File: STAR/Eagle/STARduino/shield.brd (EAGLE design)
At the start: 57.1 x 53.3 mm, 29 parts, among them U1 PCA9515A, U11 CC2, U12 SSCMNNN015PA2A3, U3 MAX31725MTA+, U5 DS3231MZ+, U7 BMX055, U8 ADXL375BCCZ

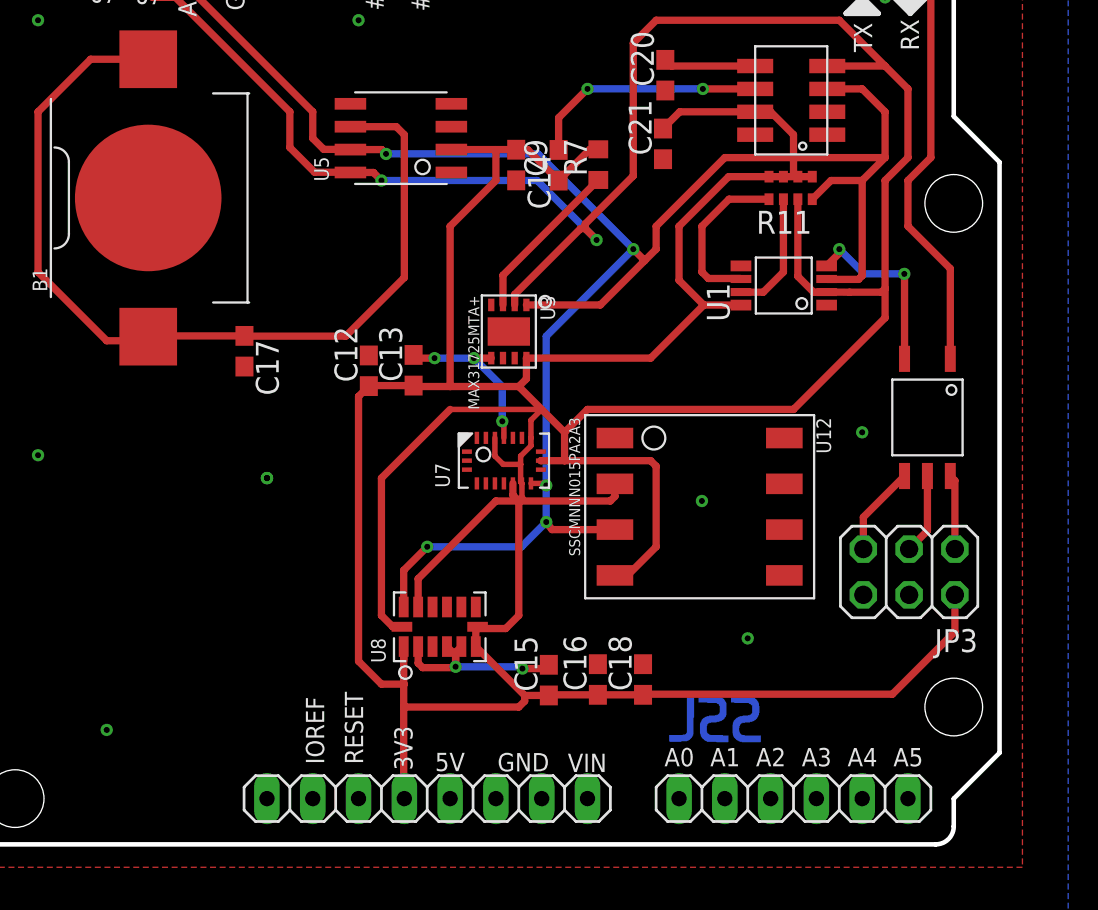
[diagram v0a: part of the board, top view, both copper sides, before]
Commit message: Fixed optoisolator circuit and added SPI header on top, but not yet the SPI head on the ICSP board. Fixed a lot of air wires
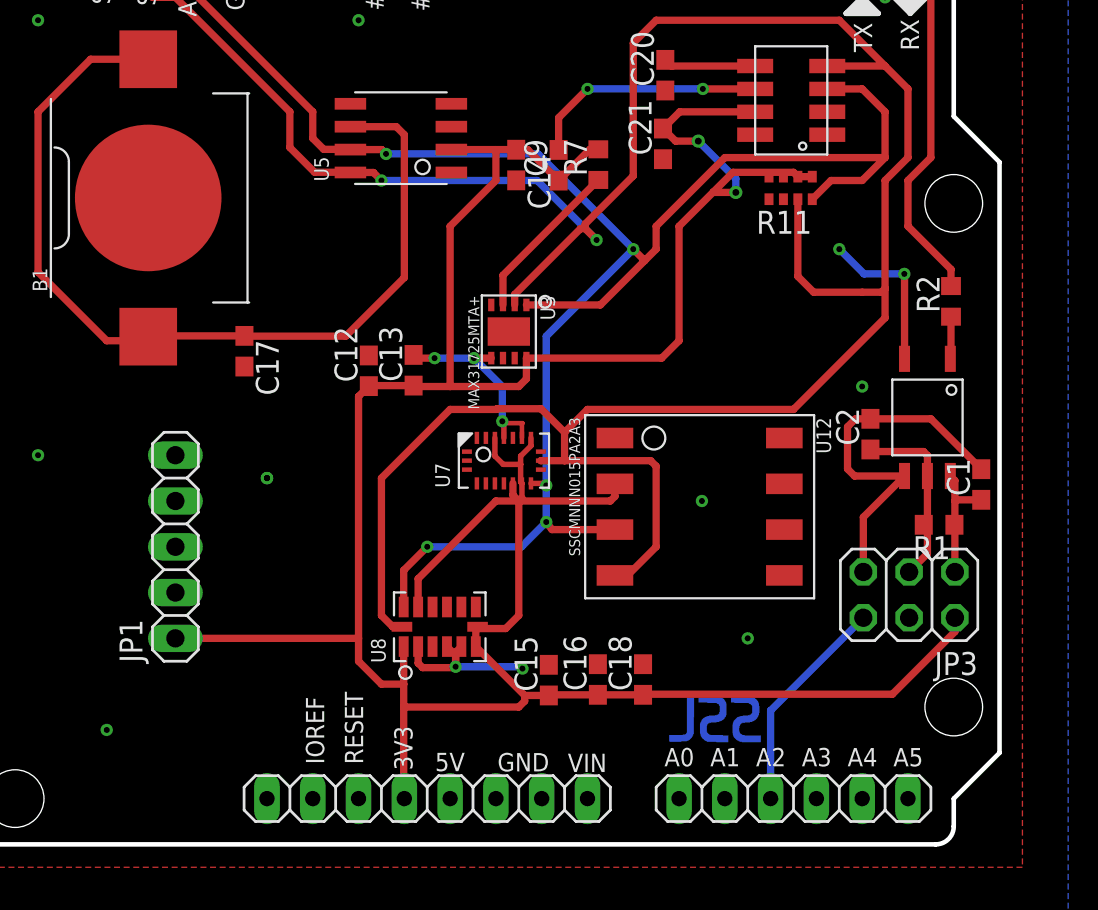
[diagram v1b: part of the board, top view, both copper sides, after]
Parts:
- removed U1: PCA9515A, CM_IC:TSSOP8
- added C1: 100nF, resistor:C0603
- added C2: 15pf, resistor:C0603
- added JP1: (no value), pinhead:1X05
- added R1, R2: 442, resistor:R0603
- moved JP3 1.27 mm to (63.6, 13.8)
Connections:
- removed net A2: AD.3
- removed net SCL_BUFF: R11.2, U1.P$7
- removed net SDA_BUFF: R11.1, U1.P$6
- new net MISO: JP1.3
- new net MOSI: JP1.4
- new net N$2: R2.1, U$3.P$1
- new net SCK: JP1.5
- net +3V3: now also JP1.1; no longer R11.7, R11.8, U1.P$8
- net BIAS_REF: now also AD.3
- net GND: now also JP1.2; no longer U1.P$4
- net MOTOR: now also R2.2; no longer U$3.P$1
- net MOTOR_GND: now also C1.2, C2.2
- net MOTOR_SIGNAL: now also C2.1, R1.2
- net MOTOR_VCC: now also C1.1, R1.1
- net SCL: no longer U1.P$2
- net SDA: no longer U1.P$3
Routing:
- net MOTOR_GND: track 5.00 -> 20.7 mm
- net BIAS_REF: track 0.00 -> 12.2 mm
- net SDA_BUFF: track 9.17 -> 0.00 mm
- net SDA: track 113.8 -> 105.0 mm
- net SCL_BUFF: track 6.86 -> 0.00 mm
- net MOTOR_SIGNAL: track 4.47 -> 10.4 mm
- net MOTOR: track 25.9 -> 21.9 mm
- net +3V3: track 173.7 -> 177.6 mm, vias 0 -> 2
- net MOTOR_VCC: track 4.16 -> 7.21 mm
- net N$2: track 0.00 -> 2.35 mm
- net GND: track 44.3 -> 43.0 mm

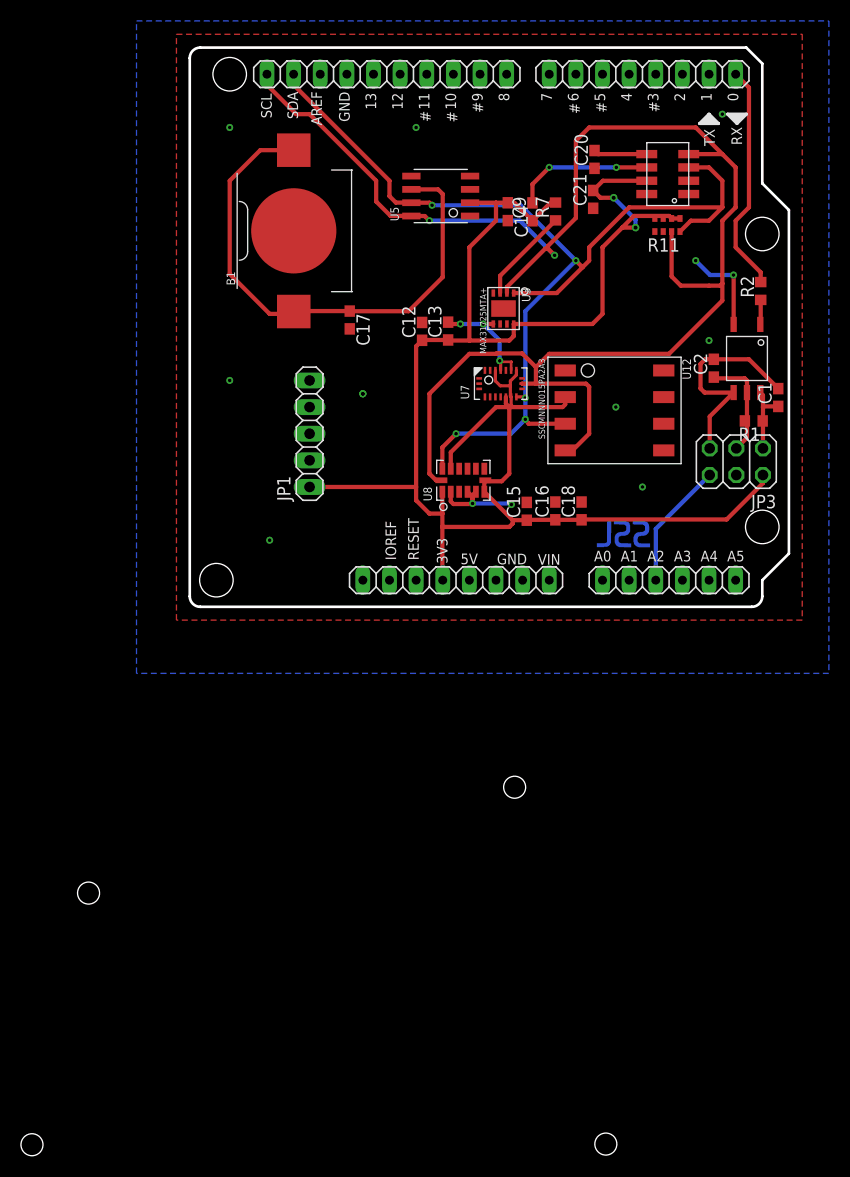
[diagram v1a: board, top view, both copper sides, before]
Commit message: Added ICSP header and finished reviewing starduino
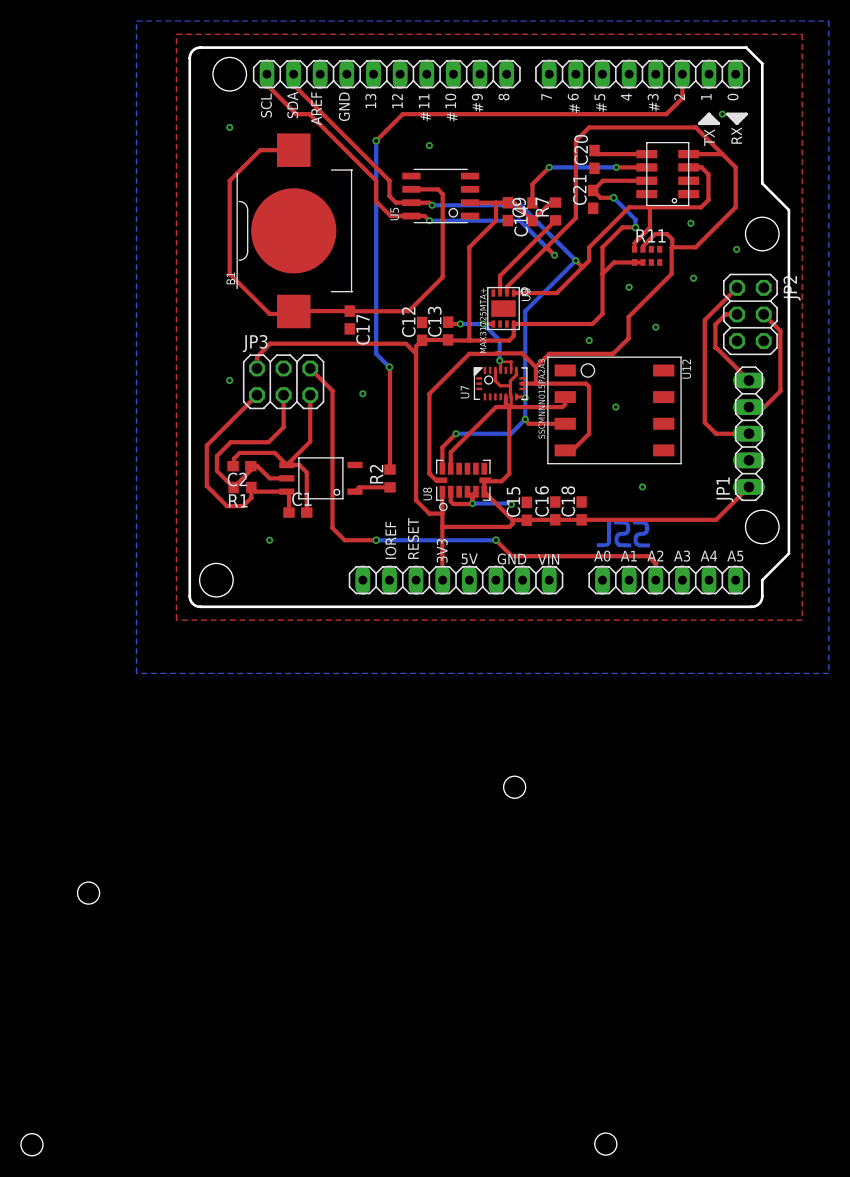
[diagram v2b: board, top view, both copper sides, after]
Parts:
- added JP2: (no value), pinhead:2X03
- moved R1 49.2 mm to (16.5, 11.4)
- moved C1 47.1 mm to (21.7, 8.99), turned to 0 degrees
- moved C2 46.0 mm to (16.4, 13.4), turned to 180 degrees
- moved JP3 43.8 mm to (20.4, 21.5), turned to 0 degrees
- moved U$3 42.2 mm to (23.9, 12.3), turned to 270 degrees
- moved JP1 41.9 mm to (64.8, 16.5)
- moved R2 39.6 mm to (30.5, 12.2)
- moved R11 3.52 mm to (55.1, 33.5), turned to 180 degrees
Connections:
- removed net D2: IOL.3
- new net D0: IOL.1
- new net ICSP2: JP2.2
- new net ICSP5: JP2.5
- net GND: now also JP2.6
- net MISO: now also JP2.1
- net MOSI: now also JP2.4
- net MOTOR: now also IOL.3; no longer IOL.1
- net SCK: now also JP2.3
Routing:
- net MOTOR: track 21.9 -> 65.1 mm, vias 0 -> 2
- net BIAS_REF: track 12.2 -> 50.0 mm, vias 0 -> 2
- net MISO: track 0.00 -> 18.8 mm
- net MOTOR_VCC: track 7.21 -> 22.6 mm
- net MOSI: track 0.00 -> 11.6 mm
- net MOTOR_SIGNAL: track 10.4 -> 21.1 mm
- net SCK: track 0.00 -> 9.19 mm
- net GND: track 43.0 -> 34.2 mm, vias 19 -> 21
- net SCL: track 155.2 -> 148.4 mm
- net SDA: track 105.0 -> 102.0 mm
- net +3V3: track 177.6 -> 180.7 mm
- net N$2: track 2.35 -> 3.51 mm
- net MOTOR_GND: track 20.7 -> 20.1 mm
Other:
- board text added: "2018STARduino Rev. 3"
- board text removed: "2018STARduino Rev. 2"

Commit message: STARduino sheild. Updated holes, resistor size, added some names to components to make assembly easier
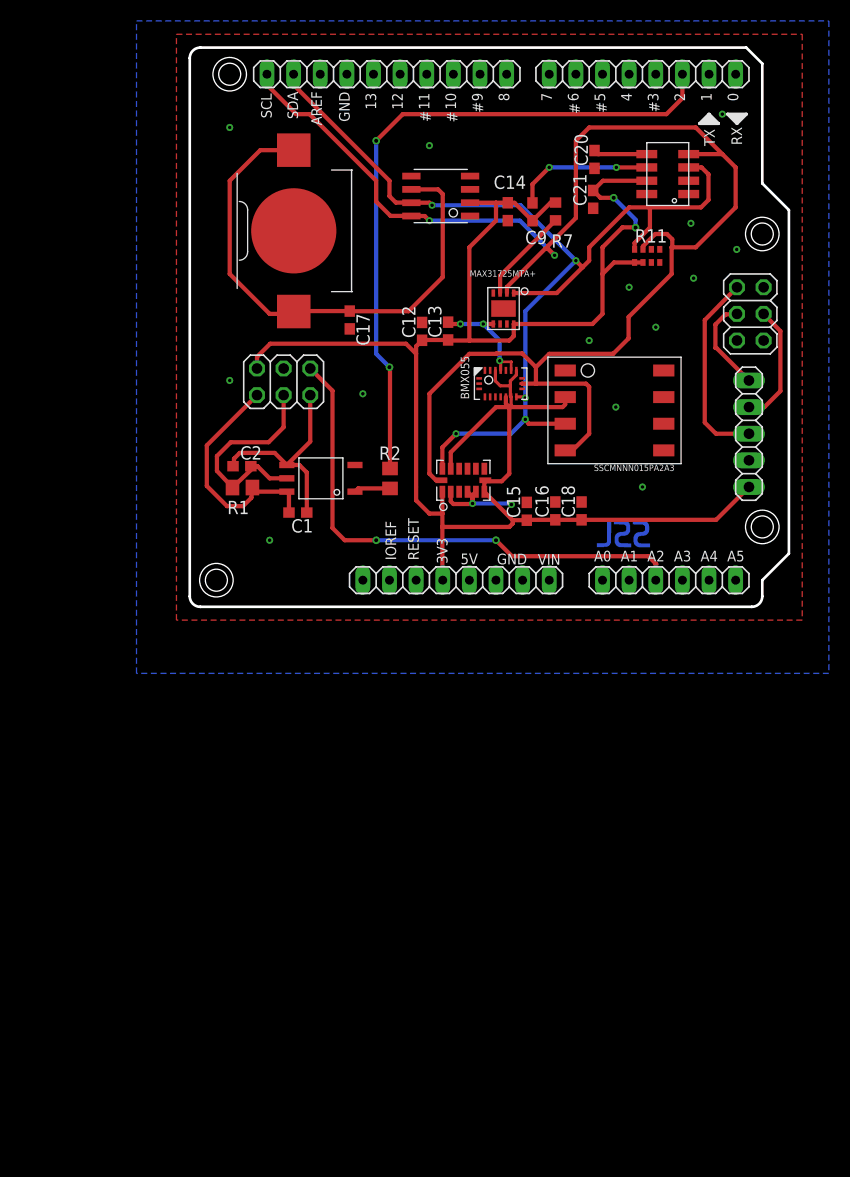
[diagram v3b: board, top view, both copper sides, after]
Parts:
- R1, R2: device resistor:R0603 -> resistor:R0805
- moved JP2 0.05 mm to (64.9, 27.9)
- renumbered U$3 to MOTORDRIVER, U11 to CC2, U3 to MAX31725MTA+, U5 to DS3231MZ+, U7 to BMX055, U8 to ADXL375BCCZ
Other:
- board text added: "Arduino M0 Shield R1"
- board text added: "UMD Nearspace ROCKSAT X"
- board text removed: "2018STARduino Rev. 3"
- board text removed: "UMD Nearspace MDSGC"
